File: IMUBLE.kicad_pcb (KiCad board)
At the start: 2 copper layers, 50 x 65 mm, 19 parts, among them SW1 SKWPACE010, U1 SL_ADXL375, U2 NJM11100, U3 SL_LSM9DS0, U4 CY8CKIT-142

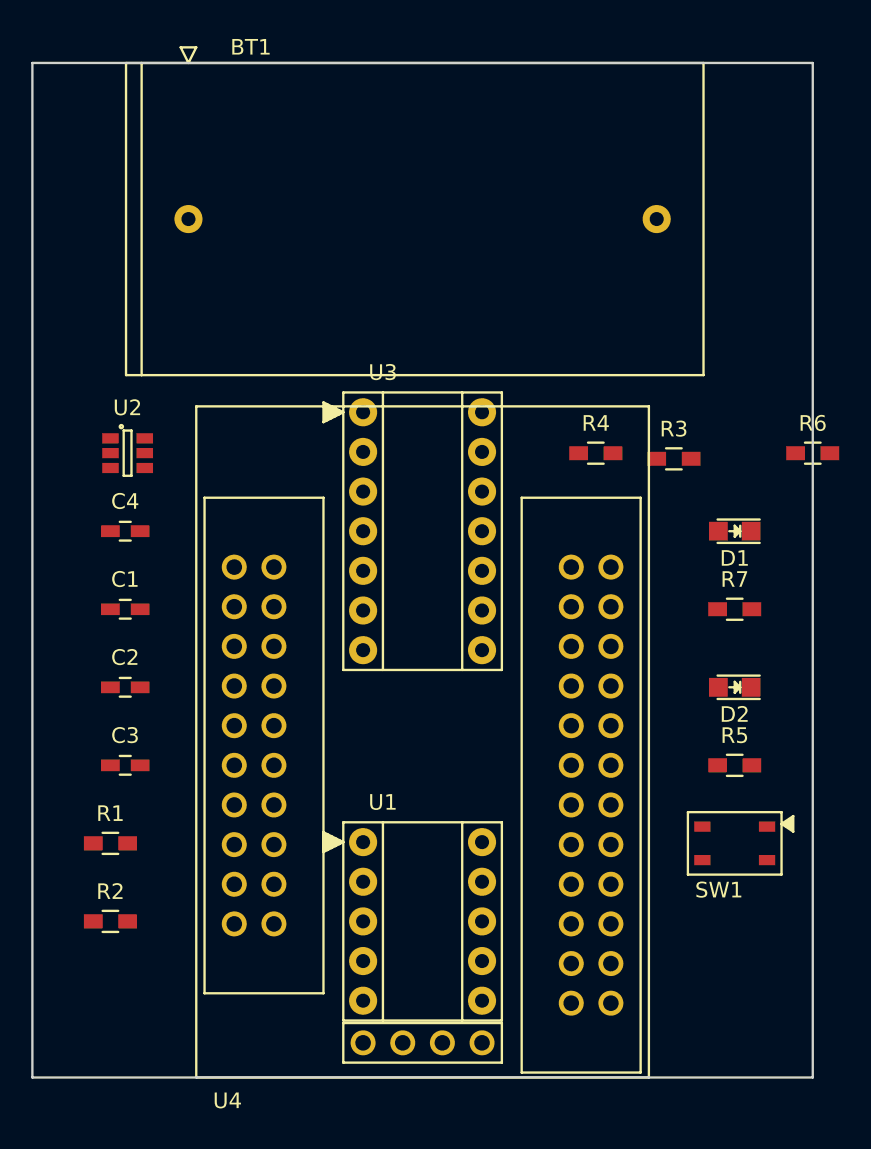
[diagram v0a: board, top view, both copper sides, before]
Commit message: Finished to layout
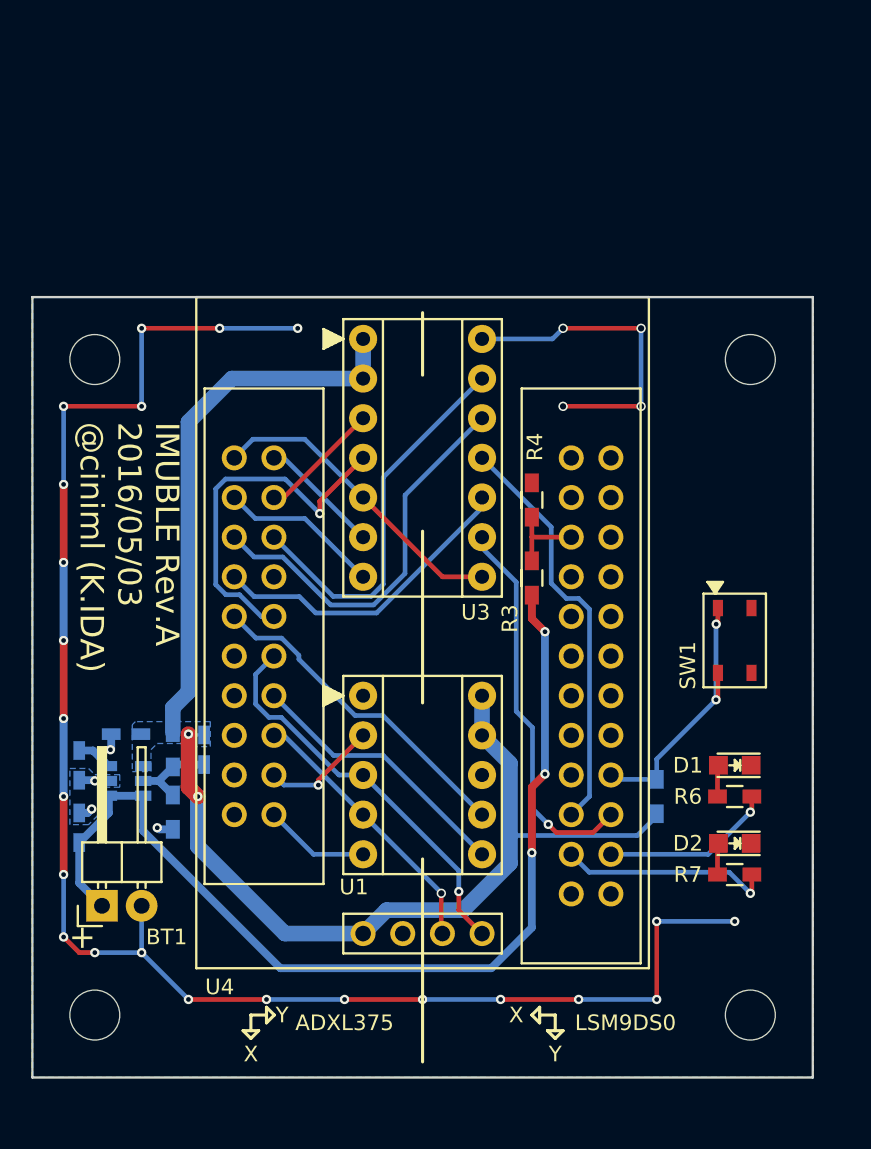
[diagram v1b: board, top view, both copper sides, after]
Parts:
- added MH1: NPTH-M3, components:NPTH-M3, F.Cu at (146.0, 54.0)
- added MH2: NPTH-M3, components:NPTH-M3, F.Cu at (146.0, 96.0)
- added MH3: NPTH-M3, components:NPTH-M3, F.Cu at (104.0, 96.0)
- added MH4: NPTH-M3, components:NPTH-M3, F.Cu at (104.0, 54.0)
- BT1: footprint components:BH-12AA-2P24 -> Pin_Headers:Pin_Header_Angled_1x02
- C1, C2, C3, C4, R1, R2, R5, U2: moved to B.Cu
- moved BT1 48.6 mm to (104.5, 89.0), turned to 90 degrees
- moved R6 22.6 mm to (145.0, 82.0), turned to 180 degrees
- moved U2 21.0 mm to (106.0, 81.0)
- moved R7 17.0 mm to (145.0, 87.0), turned to 180 degrees
- moved D1 15.0 mm to (145.0, 80.0)
- moved C1 14.3 mm to (103.0, 84.0), turned to 90 degrees
- moved C4 13.0 mm to (106.0, 78.0), turned to 180 degrees
- moved SW1 13.0 mm to (145.0, 72.0), turned to 90 degrees
- moved R3 11.9 mm to (132.0, 68.0), turned to 90 degrees
- moved D2 10.0 mm to (145.0, 85.0)
- moved U1 9.38 mm to (125.0, 80.6)
- moved R2 8.06 mm to (109.0, 83.0), turned to 270 degrees
- moved R1 7.21 mm to (109.0, 79.0), turned to 270 degrees
- moved U4 7.00 mm to (125.0, 73.0)
- moved C2 5.81 mm to (103.0, 80.0), turned to 270 degrees
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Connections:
- U4 pad 2.4: Net-(R5-Pad2) -> Net-(U4-Pad2.4)
- U4 pad 2.5: Net-(U4-Pad2.5) -> Net-(R5-Pad2)
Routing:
- net GND: track 0.00 -> 132.0 mm, vias 0 -> 31
- net +2.5V: track 0.00 -> 89.4 mm, vias 0 -> 2
- net +BATT: track 0.00 -> 64.8 mm, vias 0 -> 3
- net /LSM_DRDY: track 0.00 -> 26.7 mm
- net /ADX_MOSI: track 0.00 -> 25.6 mm, vias 0 -> 1
- net /LSM_INT1: track 0.00 -> 25.6 mm
- net /LSM_DEN: track 0.00 -> 24.9 mm, vias 0 -> 1
- net /LSM_INT2: track 0.00 -> 24.7 mm
- net /LSM_CS_XM: track 0.00 -> 23.3 mm, vias 0 -> 1
- net /ADX_INT1: track 0.00 -> 21.3 mm
- net /LSM_INTG: track 0.00 -> 20.3 mm
- net /LSM_MISO: track 0.00 -> 20.0 mm
- net /ADX_INT2: track 0.00 -> 17.5 mm
- net /ADX_MISO: track 0.00 -> 17.5 mm, vias 0 -> 1
- net Net-(R5-Pad2): track 0.00 -> 17.4 mm, vias 0 -> 2
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- added copper zone on B.Cu, net +2.5V
- added copper zone on B.Cu, net GND
- added copper zone on F.Cu, net GND
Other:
- board size 50 x 65 mm -> 50 x 50 mm
- net class Default: trace_width 0.25 -> 0.3
- board text added: "+"
- board text added: "ADXL375"
- board text added: "IMUBLE Rev.A 2016/05/03 @ciniml (K.IDA)"
- board text added: "LSM9DS0"
- board text added: "X"
- board text added: "Y"

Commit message: Remove some floating/parasistic-antenna GND patterns
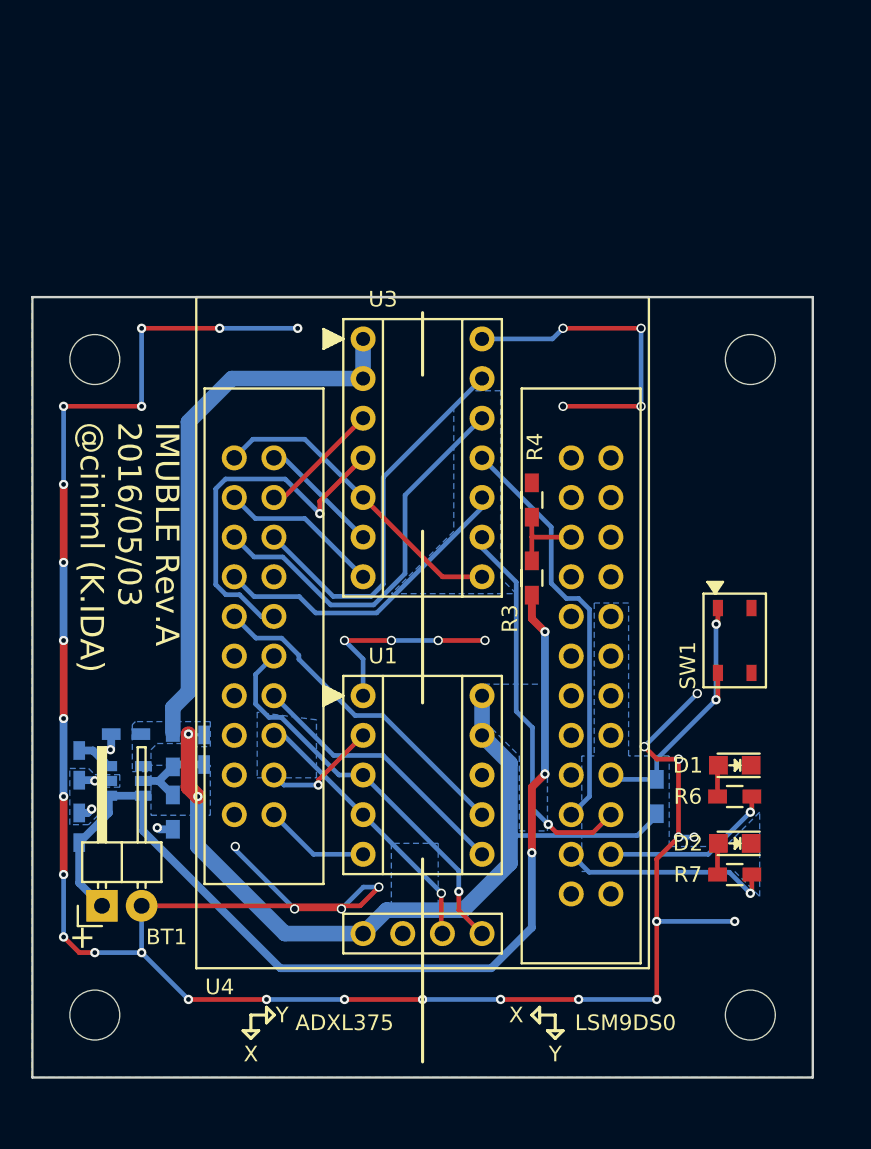
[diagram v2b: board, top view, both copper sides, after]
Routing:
- net GND: track 132.0 -> 191.6 mm, vias 31 -> 44

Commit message: Add programming signals to CY8CKIT-142
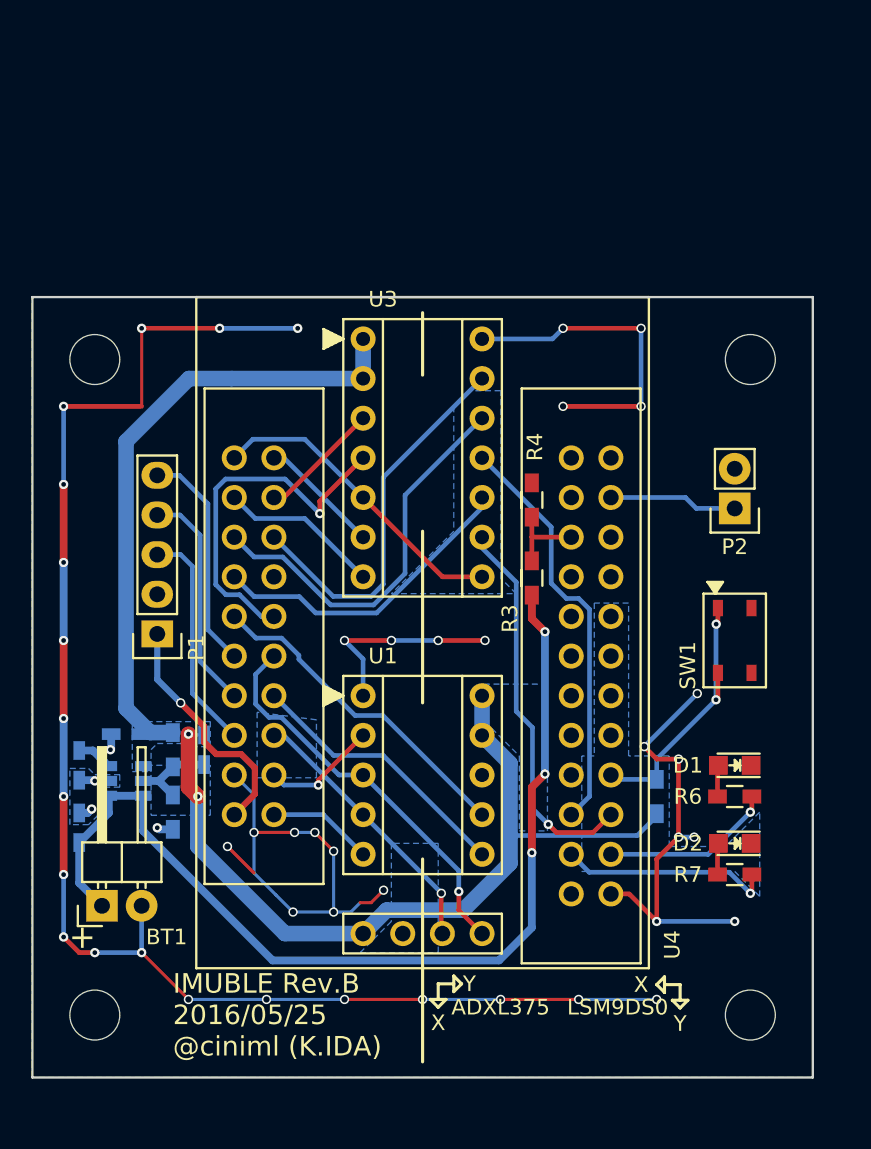
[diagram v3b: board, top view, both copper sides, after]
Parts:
- added P1: CONN_01X05, Pin_Headers:Pin_Header_Straight_1x05, F.Cu at (108.0, 71.6)
- added P2: DebugTX, Pin_Headers:Pin_Header_Straight_1x02, F.Cu at (145.0, 63.5)
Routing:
- net Net-(P1-Pad1): track 0.00 -> 15.6 mm, vias 0 -> 1
- net Net-(P1-Pad3): track 0.00 -> 14.5 mm
- net Net-(P1-Pad4): track 0.00 -> 14.5 mm
- net Net-(P1-Pad5): track 0.00 -> 14.5 mm
- net Net-(P2-Pad1): track 0.00 -> 8.22 mm
- net +2.5V: track 89.4 -> 94.3 mm
- net GND: track 191.6 -> 191.7 mm, vias 44 -> 47
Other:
- board text added: "IMUBLE Rev.B 2016/05/25 @ciniml (K.IDA)"
- board text removed: "IMUBLE Rev.A 2016/05/03 @ciniml (K.IDA)"
